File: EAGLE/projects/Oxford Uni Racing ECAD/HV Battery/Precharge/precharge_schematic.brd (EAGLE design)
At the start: 160 x 100 mm, 38 parts, among them IC1 TLV313QDCKRQ1, IC2 TLV313QDCKRQ1, U1 AMC1350QDWVRQ1AMC1350QDWVRQ1_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

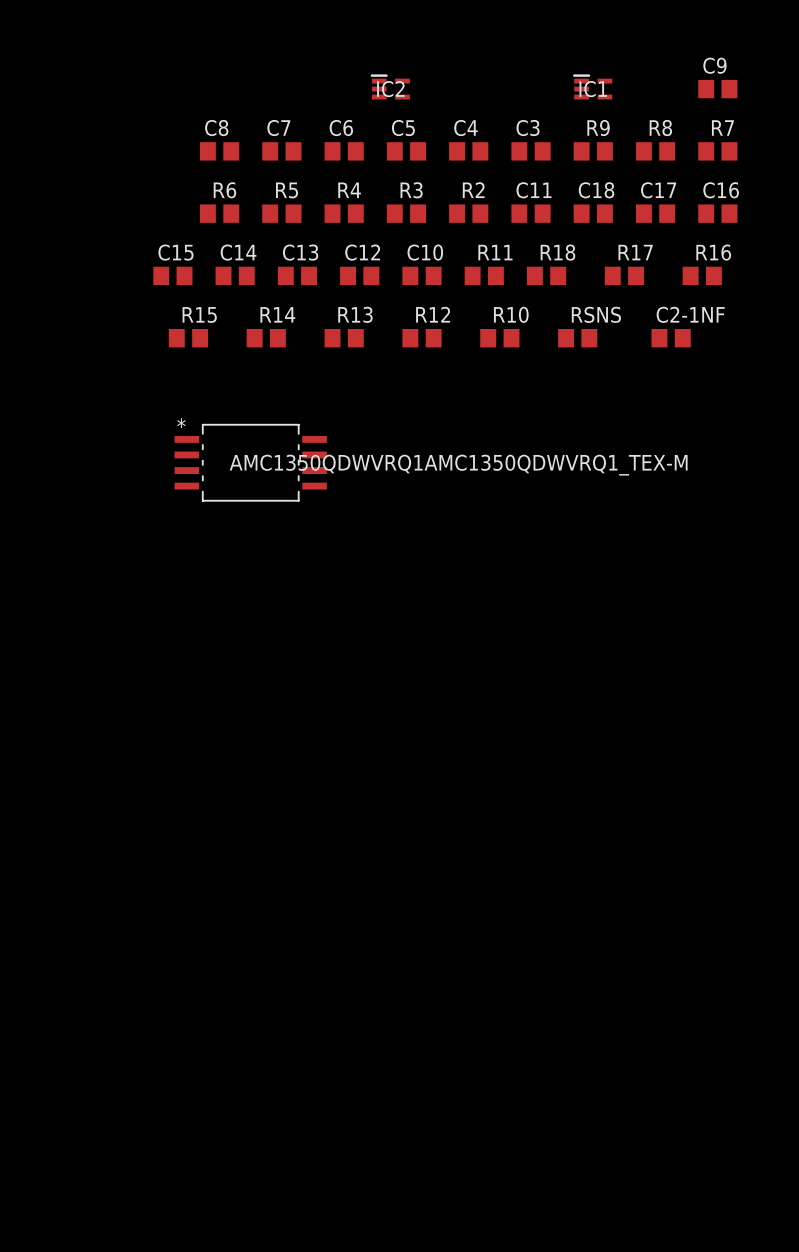
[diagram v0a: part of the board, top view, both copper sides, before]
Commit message: precharge board/ main board transfer
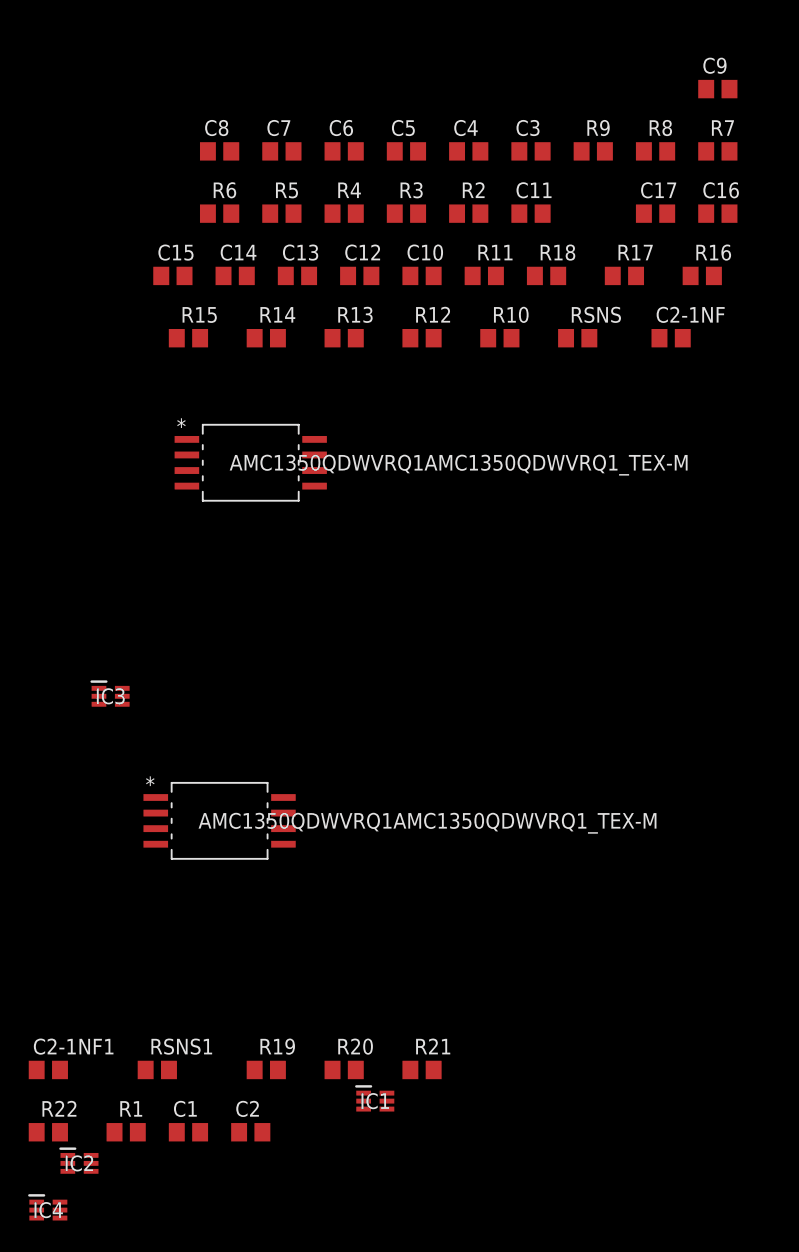
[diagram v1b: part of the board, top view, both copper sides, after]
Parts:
- removed C18: (no value), rcl:C0805
- added C1, C2, C2-1NF1: (no value), rcl:C0805
- added IC3, IC4: TLV9001SIDCKR, TLV9001SIDCKR:SOT65P210X110-6N
- added R1, R19, R20, R21, R22, RSNS1: (no value), rcl:R0805
- added U2: AMC1350QDWVRQ1AMC1350QDWVRQ1_TEX-M, AMC1350QDWVRQ1:AMC1350QDWVRQ1_TEX-M
- IC1, IC2: value TLV313QDCKRQ1 -> TLV9001SIDCKR; device TLV313QDCKRQ1:SOT65P210X110-5N -> TLV9001SIDCKR:SOT65P210X110-6N
- moved IC2 91.2 mm to (-67.3, -40.6)
- moved IC1 84.4 mm to (-43.2, -35.6)
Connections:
- new net +3V3: IC1.6, IC2.6, IC3.6, IC4.6, R14.1
- new net N$10: R19.1, U2.7
- new net N$11: R20.1, U2.6
- new net N$12: C1.2, IC1.1, R19.2, R21.2
- new net N$13: C1.1, R21.1
- new net N$14: C2.1, IC1.3, R20.2, R22.1
- new net N$15: IC2.4, R18.2
- new net N$16: C2.2, IC1.4, IC2.3, IC4.1, R15.1, R15.2, R16.1, R22.2
- new net N$17: IC4.3, R13.1, R14.2
- new net N$19: IC4.4
- new net N$3: R4.1, U1.6
- new net N$4: R3.1, U1.7
- new net N$5: R1.1, R2.1
- new net N$6: C3.2, IC3.1, R3.2, R5.2
- new net N$7: C6.1, IC3.3, R4.2, R6.1
- new net N$8: C6.2, IC2.1, IC3.4, R6.2
- new net N$9: C2-1NF1.1, R1.2, RSNS1.2, U2.2
- net GND: now also C2-1NF1.2, IC2.2, IC4.2, R13.2, R16.2, R18.1, RSNS1.1, U1.5, U2.3, U2.4, U2.5
- net N$2: now also C3.1, R5.1; no longer C12.1, C3.2
- net VDD1: now also U2.1
- net VDD2: now also U2.8

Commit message: Precharge for aminah
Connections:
- new net N$18: IC2.1, R11.1, R7.1
- net N$15: now also R7.2
- net N$8: now also R11.2; no longer IC2.1
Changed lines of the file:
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@@
 <contactref element="C6" pad="2"/>
 <contactref element="R6" pad="2"/>
-<contactref element="IC2" pad="1"/>
-<wire x1="-63.82" y1="-3.19" x2="-68.26" y2="-39.99" width="0" layer="19" extent="1-1"/>
+<contactref element="R11" pad="2"/>
 <wire x1="-54.93" y1="36.83" x2="-63.82" y2="-3.19" width="0" layer="19" extent="1-1"/>
 <wire x1="-44.77" y1="41.91" x2="-54.93" y2="36.83" width="0" layer="19" extent="1-1"/>
+<wire x1="-33.34" y1="31.75" x2="-44.77" y2="41.91" width="0" layer="19" extent="1-1"/>
 </signal>
 <signal name="N$9">
@@
 <contactref element="IC2" pad="4"/>
 <contactref element="R18" pad="2"/>
+<contactref element="R7" pad="2"/>
 <wire x1="-28.26" y1="31.75" x2="-66.36" y2="-41.29" width="0" layer="19" extent="1-1"/>
+<wire x1="-14.29" y1="41.91" x2="-28.26" y2="31.75" width="0" layer="19" extent="1-1"/>
 </signal>
 <signal name="N$17">
@@
 <contactref element="IC4" pad="4"/>
 </signal>
+<signal name="N$18">
+<contactref element="IC2" pad="1"/>
+<contactref element="R7" pad="1"/>
+<contactref element="R11" pad="1"/>
+<wire x1="-35.24" y1="31.75" x2="-68.26" y2="-39.99" width="0" layer="19" extent="1-1"/>
+<wire x1="-16.19" y1="41.91" x2="-35.24" y2="31.75" width="0" layer="19" extent="1-1"/>
+</signal>
 </signals>

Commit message: Updates to precharge schematic
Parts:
- removed C12, C15, C16, C17: (no value), rcl:C0805
- added IC10: 74HC1G86GW-Q100H, 74HC1G86GW-Q100H:SOT65P212X110-5N
- added IC11: 74LVC1G32GV,125, 74LVC1G32GV_125:SOT95P275X110-5N
- added IC5, IC6, IC7, IC8: LT1129CS8-3.3#PBF, LT1129CS8-3.3#PBF:SOIC127P599X175-8N
- added IC9: 74AHC1G08GV,125, 74AHC1G08GV_125:SOT95P275X110-5N
- added J1: T816108A1S102CEU, T816108A1S102CEU:T816108A1S102CEU
- added PS1, PS2: PDSE1-S12-S5-M-TR, PDSE1-S12-S5-M-TR:PDSE1S12S5MTR
- added Q1, Q2: BSS138, BSS138:SOT95P240X120-3N
- added R23, R24: (no value), rcl:R0805
- moved C9 247.4 mm to (-80.0, -191.8)
- moved C11 240.6 mm to (-105.4, -191.8)
- moved C8 235.5 mm to (-85.1, -191.8)
- moved C10 234.6 mm to (-110.5, -191.8)
- moved IC1 170.1 mm to (-104.1, -194.3)
- moved R19 161.5 mm to (-101.6, -186.7)
- moved R20 161.5 mm to (-95.2, -186.7)
- moved R21 161.5 mm to (-88.9, -186.7)
- moved RSNS1 161.5 mm to (-110.5, -186.7)
- moved C1 158.0 mm to (-95.2, -191.8)
- moved C2 158.0 mm to (-90.2, -191.8)
- moved R1 158.0 mm to (-100.3, -191.8)
- moved R22 149.1 mm to (-82.5, -186.7)
- moved U2 143.9 mm to (-95.2, -151.1)
- moved C2-1NF1 138.5 mm to (-72.4, -171.4)
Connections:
- removed net N$5 (its old number): R1.1, R2.1
- removed net VDD1: U1.1, U2.1
- removed net VDD2: U1.8, U2.8
- new net +12V: IC7.8, IC8.8, Q2.3
- new net CHARGE_POWER: IC6.8
- new net N$13: C8.1, IC1.3, R20.2, R22.1
- new net N$20: C14.2
- new net N$21: C5.2
- new net N$22: C13.2, C7.2, PS2.5, R12.1, U1.1
- new net N$23: PS2.4, R10.2
- new net N$24: IC7.1, PS2.2
- new net N$25: R10.1, R12.2
- new net N$26: C11.2
- new net N$27: C2.2
- new net N$28: C10.2, C9.2, PS1.5, R24.1, U2.1
- new net N$29: PS1.4, R23.2
- new net N$30: IC8.1, PS1.2
- new net N$31: R23.1, R24.2
- new net N$32: IC10.2, IC6.1
- new net N$33: IC10.1, IC5.1
- new net N$34: IC10.4, IC9.2
- new net N$35: IC9.4, Q2.1
- new net N$36: IC6.6, IC6.7
- new net N$37: IC5.6, IC5.7
- new net N$38: IC11.4, Q1.1
- new net N$40: J1.1, Q1.3
- new net READY_POWER: IC5.8
- net +3V3: now also C11.1, C14.1, C2.1, C5.1, IC10.5, IC11.5, IC9.5, U1.8, U2.8
- net GND: now also C10.1, C13.1, C7.1, C9.1, IC10.3, IC11.3, IC5.3, IC6.3, IC7.3, IC7.6, IC7.7, IC8.3, IC8.6, IC8.7, IC9.3, PS1.1, PS2.1, Q1.2, Q2.2
- net N$14: now also C8.2, IC1.4, R22.2; no longer C2.1, IC1.3, R20.2, R22.1
- net N$15: now also IC11.2
- net N$16: no longer C2.2, IC1.4, R22.2
- net N$19: now also IC9.1

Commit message: first precharge brd deisgn,
need to fix TS/LV separation and add annotation
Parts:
- added TP1, TP2: PTR1PAD1-17, testpad:P1-17
- moved IC1 258.4 mm to (47.0, 15.2)
- moved C1 256.9 mm to (53.3, 17.8)
- moved PS1 254.0 mm to (49.5, 27.9)
- moved C11 251.6 mm to (27.9, 21.6)
- moved IC11 251.6 mm to (68.5, 45.8)
- moved C10 249.2 mm to (20.3, 20.3), turned to 180 degrees
- moved R19 248.0 mm to (40.6, 16.5)
- moved Q2 248.0 mm to (73.7, 27.9)
- moved R21 247.0 mm to (53.3, 15.2)
- moved RSNS1 244.0 mm to (10.2, 25.4), turned to 270 degrees
- moved R20 242.3 mm to (40.6, 14.0)
- moved C2 241.7 mm to (27.9, 19.1)
- moved C8 241.6 mm to (49.5, 8.89)
- moved R1 240.8 mm to (12.2, 21.1), turned to 90 degrees
- moved R22 238.5 mm to (48.3, 12.7)
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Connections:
- removed net N$12: C1.1, R21.1
- removed net N$14: C8.2, IC1.4, R22.2
- removed net N$2 (its old number): C3.1, R5.1
- removed net N$20: C14.2
- removed net N$21: C5.2
- removed net N$26: C11.2
- removed net N$27: C2.2
- new net GND1: C2-1NF.2, RSNS.1, U1.3, U1.4
- new net GND2: C2-1NF1.2, RSNS1.1, U2.3, U2.4
- net GND: now also C1.1, C11.2, C14.2, C2.2, C3.1, C5.2, R21.1, R5.1; no longer C2-1NF.2, C2-1NF1.2, RSNS.1, RSNS1.1, U1.3, U1.4, U2.3, U2.4
- net N$16: now also C8.2, IC1.4, R22.2
- net N$5: now also TP1.TP
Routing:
- net GND: track 0.00 -> 164.6 mm, vias 0 -> 22
- net N$32: track 0.00 -> 121.9 mm
- net N$33: track 0.00 -> 107.5 mm
- net N$22: track 0.00 -> 55.7 mm
- net N$28: track 0.00 -> 53.8 mm
- net N$16: track 0.00 -> 52.6 mm
- net +3V3: track 0.00 -> 44.2 mm, vias 0 -> 10
- net N$8: track 0.00 -> 37.3 mm
- net N$23: track 0.00 -> 30.6 mm
- net N$29: track 0.00 -> 29.4 mm
- net N$24: track 0.00 -> 24.8 mm
- net N$30: track 0.00 -> 22.6 mm
- net N$13: track 0.00 -> 21.2 mm
- net N$6: track 0.00 -> 19.0 mm
- net N$5: track 0.00 -> 18.2 mm
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- added copper zone on layer 15, net +12V
- added copper zone on layer 15, net +3V3
- added copper zone on layer 2, net GND
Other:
- board size 160 x 100 mm -> 94 x 72.4 mm

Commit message: Second Precharge board
Fixes the TS-LV separation and changes from 4 layer board to 2 layer board.
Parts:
- moved TP2 192.7 mm to (-21.6, 73.7)
- moved IC6 72.9 mm to (78.7, 15.2)
- moved IC5 72.4 mm to (78.7, 8.89)
- moved C4 65.9 mm to (-86.4, 83.8)
- moved TP1 64.8 mm to (-16.5, 73.7)
- moved R8 58.4 mm to (-61.0, 83.8)
- moved R9 58.4 mm to (-66.0, 83.8)
- moved R17 47.0 mm to (-22.9, 78.7)
- moved PS1 27.7 mm to (22.9, 20.3), turned to 90 degrees
- moved PS2 27.1 mm to (22.9, 55.9), turned to 90 degrees
- moved Q1 20.7 mm to (72.4, 33.0)
- moved RSNS1 18.5 mm to (5.08, 7.62), turned to 90 degrees
- moved C2-1NF1 17.8 mm to (12.7, 7.62), turned to 270 degrees
- moved R10 16.9 mm to (12.7, 63.5)
- moved RSNS 15.5 mm to (6.35, 40.6), turned to 90 degrees
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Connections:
- net +3V3 renamed 3V3
- net GND: no longer C10.1, C13.1, C7.1, C9.1
- net GND1: now also C13.1, C7.1
- net GND2: now also C10.1, C9.1
- net N$5: no longer TP1.TP
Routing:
- net +12V: track 5.70 -> 126.5 mm
- net N$32: track 121.9 -> 5.27 mm
- net N$33: track 107.5 -> 5.00 mm
- net GND: track 164.6 -> 118.2 mm, vias 22 -> 20
- net N$22: track 55.7 -> 27.5 mm
- net N$28: track 53.8 -> 26.5 mm
- net GND2: track 3.81 -> 27.9 mm, vias 0 -> 2
- net N$29: track 29.4 -> 5.73 mm
- net N$8: track 37.3 -> 16.2 mm
- net N$40: track 11.8 -> 31.0 mm
- net 3V3: track 44.2 -> 61.8 mm
- net N$24: track 24.8 -> 10.4 mm
- net N$23: track 30.6 -> 16.8 mm
- net N$30: track 22.6 -> 10.3 mm
- net GND1: track 13.7 -> 24.9 mm, vias 0 -> 2
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- added copper zone on layer 16, net 3V3
- added copper zone on layer 16, net GND
- added copper zone on layer 16, net GND1
- added copper zone on layer 16, net GND2
- removed copper zone on layer 15, net +12V
- removed copper zone on layer 15, net 3V3
- removed copper zone on layer 2, net GND
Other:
- board size 94 x 72.4 mm -> 87.6 x 70.8 mm

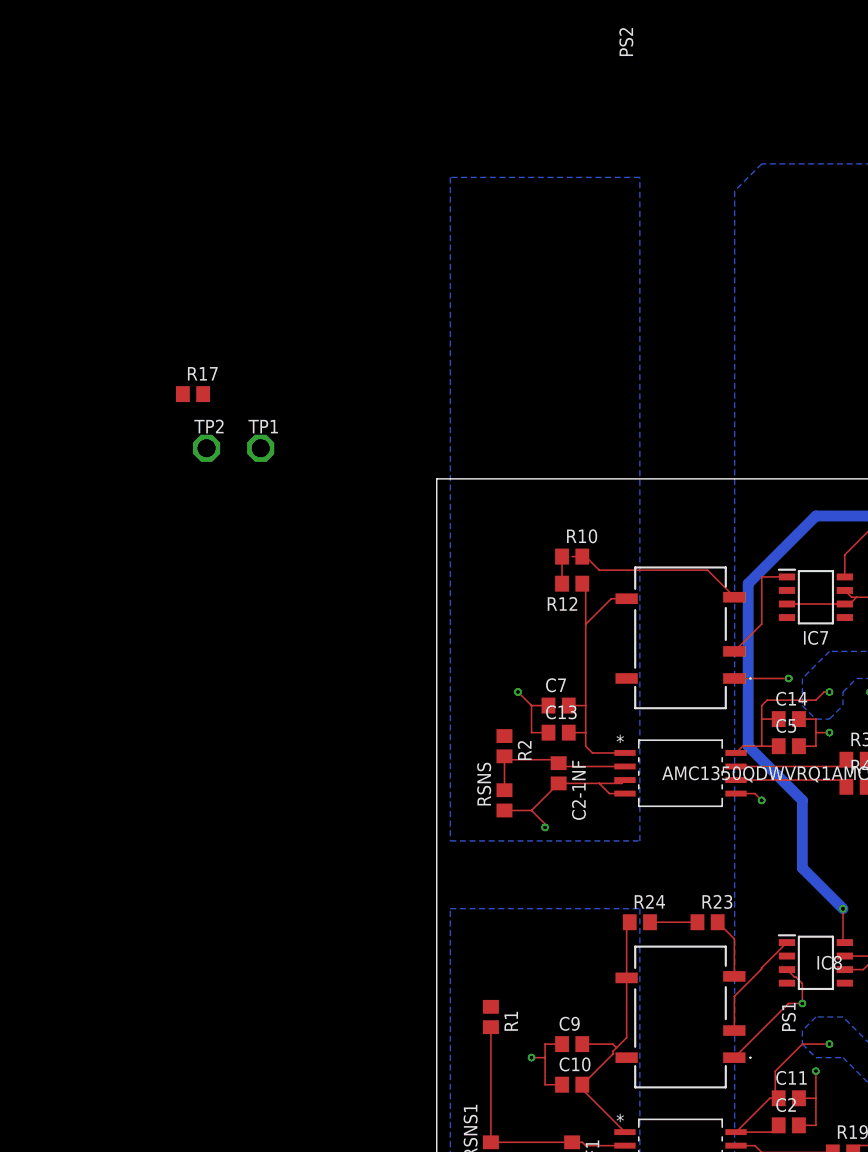
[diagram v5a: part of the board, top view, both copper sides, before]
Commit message: Updated precharge board
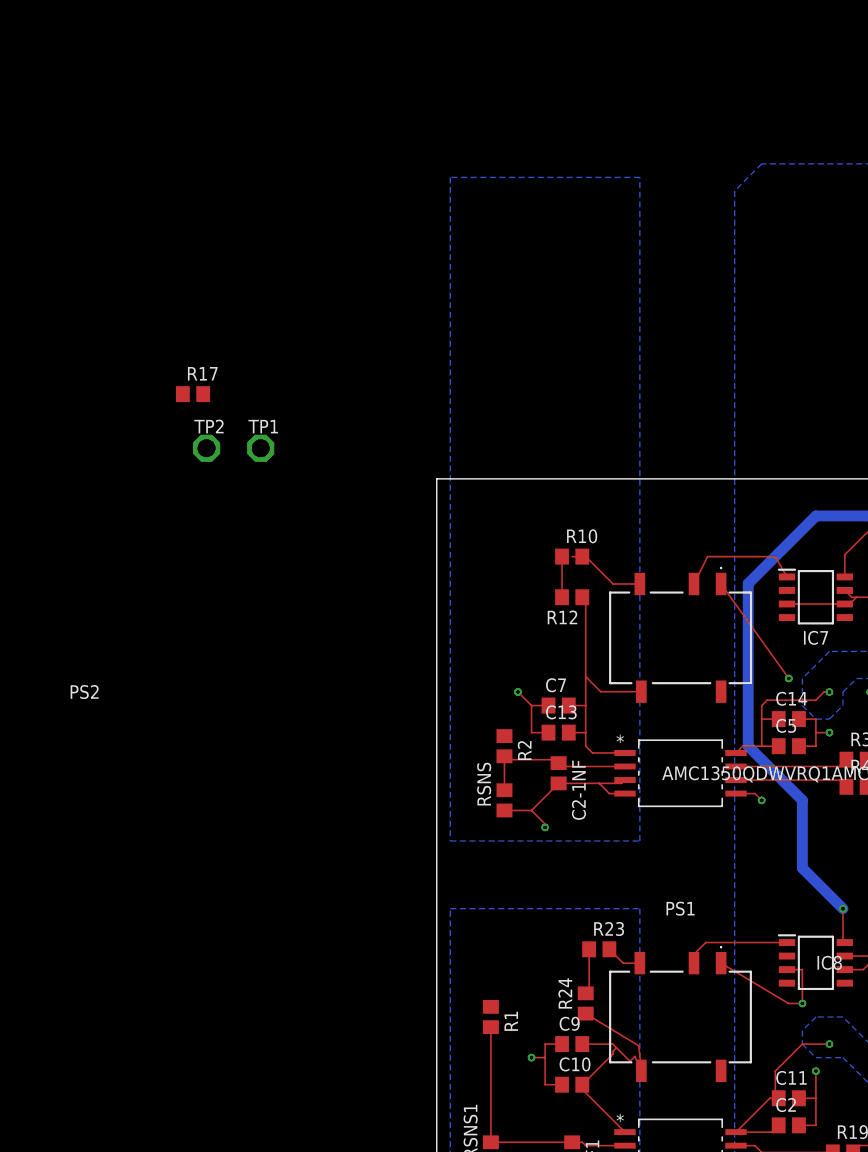
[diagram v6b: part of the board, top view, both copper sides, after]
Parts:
- moved R23 10.5 mm to (15.2, 26.7)
- moved R24 9.16 mm to (14.0, 21.6), turned to 90 degrees
- moved R12 1.27 mm to (12.7, 59.7)
- turned PS1 to 180 degrees
- turned PS2 to 180 degrees
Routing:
- net N$23: track 16.8 -> 7.41 mm
- net GND: track 118.2 -> 125.0 mm
- net N$29: track 5.73 -> 3.40 mm
- net N$25: track 2.54 -> 3.81 mm
- net N$24: track 10.4 -> 11.4 mm
